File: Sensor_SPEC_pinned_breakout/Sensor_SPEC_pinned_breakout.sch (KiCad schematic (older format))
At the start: 5 parts, among them U1 SPEC, U2 SMM-102-02-S-S, U3 SMM-102-02-S-S, U4 SMM-102-02-S-S

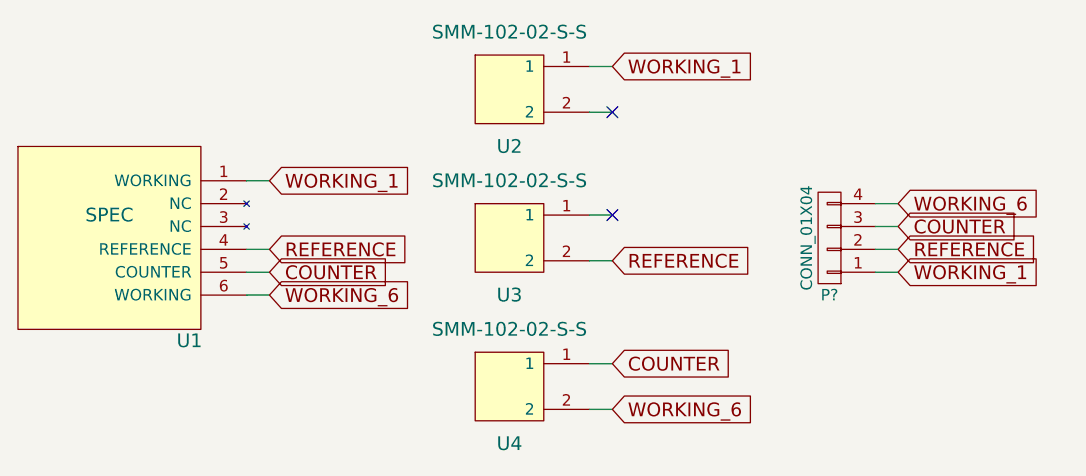
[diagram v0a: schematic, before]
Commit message: changed SPEC pinned breakout
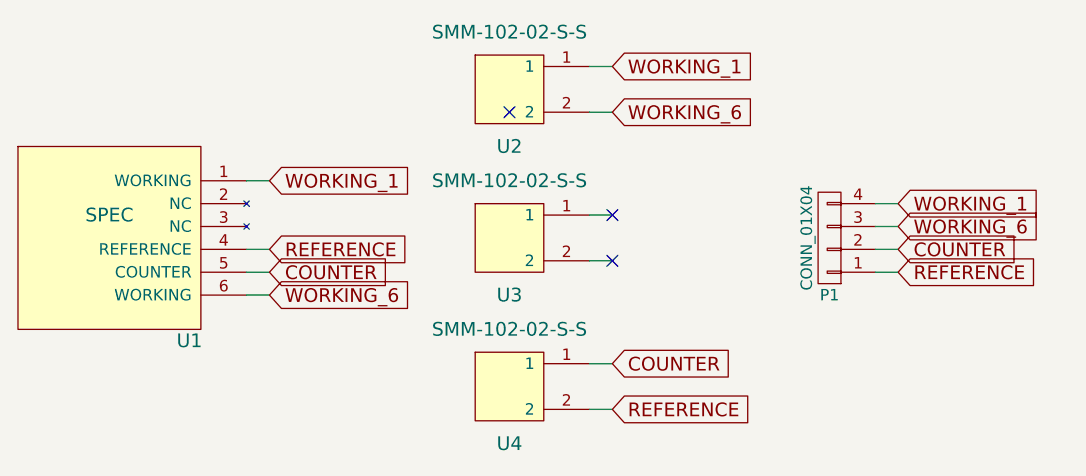
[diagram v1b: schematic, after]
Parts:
- P1: renamed from P?; footprint (none) -> Socket_Strips:Socket_Strip_Straight_1x04
- U1: footprint (none) -> scintilla:SPEC_pinned
- U2, U3, U4: footprint (none) -> scintilla:SMM-102-02-S-S
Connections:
- net COUNTER: now also P1.2 (P2); no longer P1.3 (P3)
- net REFERENCE: now also P1.1 (P1), U4.2; no longer P1.2 (P2), U3.2
- net WORKING_1: now also P1.4 (P4); no longer P1.1 (P1)
- net WORKING_6: now also P1.3 (P3), U2.2; no longer P1.4 (P4), U4.2
- no-connect marks 2 -> 3
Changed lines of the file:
@@
 F 0 "U1" H 5950 3350 60  0000 C CNN
 F 1 "SPEC" H 5600 3900 60  0000 C CNN
-F 2 "" H 5600 3800 60  0001 C CNN
+F 2 "scintilla:SPEC_pinned" H 5600 3800 60  0001 C CNN
 F 3 "" H 5600 3800 60  0001 C CNN
 	1    5600 3800
@@
 F 0 "U2" H 7350 2900 60  0000 C CNN
 F 1 "SMM-102-02-S-S" H 7350 3400 60  0000 C CNN
-F 2 "" H 7350 3150 60  0001 C CNN
+F 2 "scintilla:SMM-102-02-S-S" H 7350 3150 60  0001 C CNN
 F 3 "" H 7350 3150 60  0001 C CNN
 	1    7350 3150
@@
 F 0 "U3" H 7350 3550 60  0000 C CNN
 F 1 "SMM-102-02-S-S" H 7350 4050 60  0000 C CNN
-F 2 "" H 7350 3800 60  0001 C CNN
+F 2 "scintilla:SMM-102-02-S-S" H 7350 3800 60  0001 C CNN
 F 3 "" H 7350 3800 60  0001 C CNN
 	1    7350 3800
@@
 F 0 "U4" H 7350 4200 60  0000 C CNN
 F 1 "SMM-102-02-S-S" H 7350 4700 60  0000 C CNN
-F 2 "" H 7350 4450 60  0001 C CNN
+F 2 "scintilla:SMM-102-02-S-S" H 7350 4450 60  0001 C CNN
 F 3 "" H 7350 4450 60  0001 C CNN
 	1    7350 4450
@@
 Text GLabel 7800 3050 2    60   Input ~ 0
 WORKING_1
-NoConn ~ 7800 3250
 NoConn ~ 7800 3700
-Text GLabel 7800 3900 2    60   Input ~ 0
+Text GLabel 7800 4550 2    60   Input ~ 0
 REFERENCE
 Text GLabel 7800 4350 2    60   Input ~ 0
 COUNTER
-Text GLabel 7800 4550 2    60   Input ~ 0
+Text GLabel 7800 3250 2    60   Input ~ 0
 WORKING_6
 $Comp
-L CONN_01X04 P?
+L CONN_01X04 P1
 U 1 1 57C09EF5
 P 8750 3800
-F 0 "P?" H 8750 4050 50  0000 C CNN
+F 0 "P1" H 8750 4050 50  0000 C CNN
 F 1 "CONN_01X04" V 8850 3800 50  0000 C CNN
-F 2 "" H 8750 3800 50  0000 C CNN
+F 2 "Socket_Strips:Socket_Strip_Straight_1x04" H 8750 3800 50  0001 C CNN
 F 3 "" H 8750 3800 50  0000 C CNN
 	1    8750 3800
@@
 Wire Wire Line
 	8950 3650 9050 3650
+Text GLabel 9050 3650 2    60   Input ~ 0
+WORKING_1
 Text GLabel 9050 3950 2    60   Input ~ 0
-WORKING_1
+REFERENCE
 Text GLabel 9050 3850 2    60   Input ~ 0
-REFERENCE
+COUNTER
 Text GLabel 9050 3750 2    60   Input ~ 0
-COUNTER
-Text GLabel 9050 3650 2    60   Input ~ 0
 WORKING_6
+NoConn ~ 7800 3900
+NoConn ~ 7350 3250
 $EndSCHEMATC
